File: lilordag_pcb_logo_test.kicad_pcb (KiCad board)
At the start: 2 copper layers, 98.1 x 100 mm, 178 parts, among them J1 USB4105-GF-A, J2 826629-7, J3 826629-7, Q1 BC846, Q2 BC846, Q3 MMBT3906, Q4 MMBT3906, Q5 BC846, Q6 BC846, Q7 SSM3J56MFV, Q8 SSM3J56MFV, SW1 PCM12SMTR, SW2 PCM12SMTR, SW3 SW_MEC_5G, SW4 PCM12SMTR, SW5 SW_MEC_5G, SW6 SW_MEC_5G, SW7 SW_MEC_5G, U1 ESP32-C3-MINI-1-N4, U2 WS2812B-B, U3 WS2812B-B, U4 WS2812B-B, U5 WS2812B-B

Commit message: Logos locked
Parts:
- moved Ref** 23.2 mm to (76.9, 123.0)
- moved Ref** 16.1 mm to (77.0, 103.2)
- moved Ref** 5.02 mm to (89.4, 91.5)
- moved Ref** 4.76 mm to (111.7, 91.5)
- moved Ref** 4.67 mm to (66.3, 91.5)
- moved Ref** 4.47 mm to (95.2, 77.2)
- moved Ref** 4.47 mm to (117.6, 77.2)
- moved Ref** 4.16 mm to (43.5, 91.5)
- moved Ref** 4.13 mm to (72.1, 77.2)
- moved Ref** 4.08 mm to (49.5, 77.2)
- moved Ref** 1.27 mm to (77.0, 112.5)
- moved Ref** 0.12 mm to (55.2, 114.0)
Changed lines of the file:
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@@
     )
   )
-  (footprint "pcb_logos:candy-simple-light-green" (layer "F.Cu")
-    (at 71.628 73.152)
+  (footprint "pcb_logos:candy-simple-light-green" locked (layer "F.Cu")
+    (at 72.1 77.25)
     (attr through_hole)
     (fp_text reference "Ref**" (at 0 0) (layer "F.SilkS") hide
@@
       ) (layer "F.Cu") (width 0.01) (fill solid))
   )
-  (footprint "pcb_logos:candy-simple-white" (layer "F.Cu")
-    (at 49.45 73.168839)
+  (footprint "pcb_logos:candy-simple-white" locked (layer "F.Cu")
+    (at 49.45 77.25)
     (attr through_hole)
     (fp_text reference "Ref**" (at 0 0) (layer "F.SilkS") hide
@@
     )
   )
-  (footprint "pcb_logos:drawing" (layer "F.Cu")
-    (at 76.962 99.822)
+  (footprint "pcb_logos:drawing" locked (layer "F.Cu")
+    (at 76.9 123)
     (attr through_hole)
     (fp_text reference "Ref**" (at 0 0) (layer "F.SilkS") hide
@@
     )
   )
-  (footprint "pcb_logos:candy-simple-clear" (layer "F.Cu")
-    (at 116.586 72.898)
+  (footprint "pcb_logos:candy-simple-clear" locked (layer "F.Cu")
+    (at 117.6 77.25)
     (attr through_hole)
     (fp_text reference "Ref**" (at 0 0) (layer "F.SilkS") hide
@@
     )
   )
-  (footprint "pcb_logos:simple_tower_7x7" (layer "F.Cu")
-    (at 77.216 111.252)
+  (footprint "pcb_logos:simple_tower_7x7" locked (layer "F.Cu")
+    (at 77 112.5)
     (attr through_hole)
     (fp_text reference "Ref**" (at 0 0) (layer "F.SilkS") hide
@@
     )
   )
-  (footprint "pcb_logos:tower-complex-gold" (layer "F.Cu")
-    (at 90.654962 86.684281)
+  (footprint "pcb_logos:tower-complex-gold" locked (layer "F.Cu")
+    (at 89.4 91.54)
     (attr through_hole)
     (fp_text reference "Ref**" (at 0 0) (layer "F.SilkS") hide
@@
       (net 79 "Net-(TP15-Pad1)") (pinfunction "DIN") (pintype "input"))
   )
-  (footprint "pcb_logos:candy-simple-gold" (layer "F.Cu")
-    (at 96.254379 72.894768)
+  (footprint "pcb_logos:candy-simple-gold" locked (layer "F.Cu")
+    (at 95.25 77.25)
     (attr through_hole)
     (fp_text reference "Ref**" (at 0 0) (layer "F.SilkS") hide
@@
     (pad "" np_thru_hole circle locked (at 0 0) (size 6 6) (drill 6) (layers *.Cu *.Mask))
   )
-  (footprint "pcb_logos:tower-complex-clear" (layer "F.Cu")
-    (at 110.722834 86.879447)
+  (footprint "pcb_logos:tower-complex-clear" locked (layer "F.Cu")
+    (at 111.7 91.54)
     (attr through_hole)
     (fp_text reference "Ref**" (at 0 0) (layer "F.SilkS") hide
@@
     )
   )
-  (footprint "pcb_logos:tower-complex-white" (layer "F.Cu")
-    (at 43.45 87.376)
+  (footprint "pcb_logos:tower-complex-white" locked (layer "F.Cu")
+    (at 43.45 91.54)
     (attr through_hole)
     (fp_text reference "Ref**" (at 0 0) (layer "F.SilkS") hide
@@
   )
   (footprint "pcb_logos:tower-complex-light-green-stars" locked (layer "F.Cu")
-    (at 55.1 114)
+    (at 55.225 114)
     (attr through_hole)
     (fp_text reference "Ref**" (at 0 0) (layer "F.SilkS") hide
@@
     )
   )
-  (footprint "pcb_logos:tower-complex-light-green" (layer "F.Cu")
-    (at 66.294 86.868)
+  (footprint "pcb_logos:tower-complex-light-green" locked (layer "F.Cu")
+    (at 66.3 91.54)
     (attr through_hole)
     (fp_text reference "Ref**" (at 0 0) (layer "F.SilkS") hide
@@
       ) (layer "F.Cu") (width 0.01) (fill solid))
   )
-  (footprint "pcb_logos:simple_tower_5x5" (layer "F.Cu")
-    (at 76.962 119.38)
+  (footprint "pcb_logos:simple_tower_5x5" locked (layer "F.Cu")
+    (at 77 103.25)
     (attr through_hole)
     (fp_text reference "Ref**" (at 0 0) (layer "F.SilkS") hide

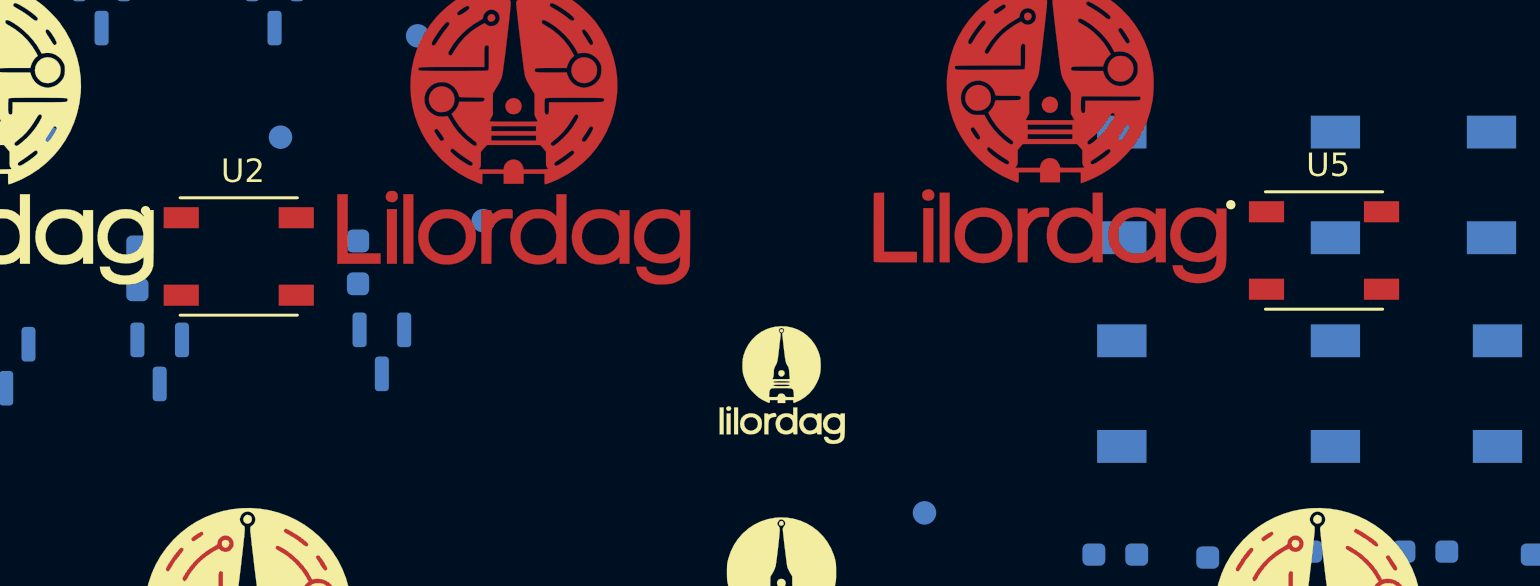
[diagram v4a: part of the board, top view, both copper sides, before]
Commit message: Added 3d model for RGBs
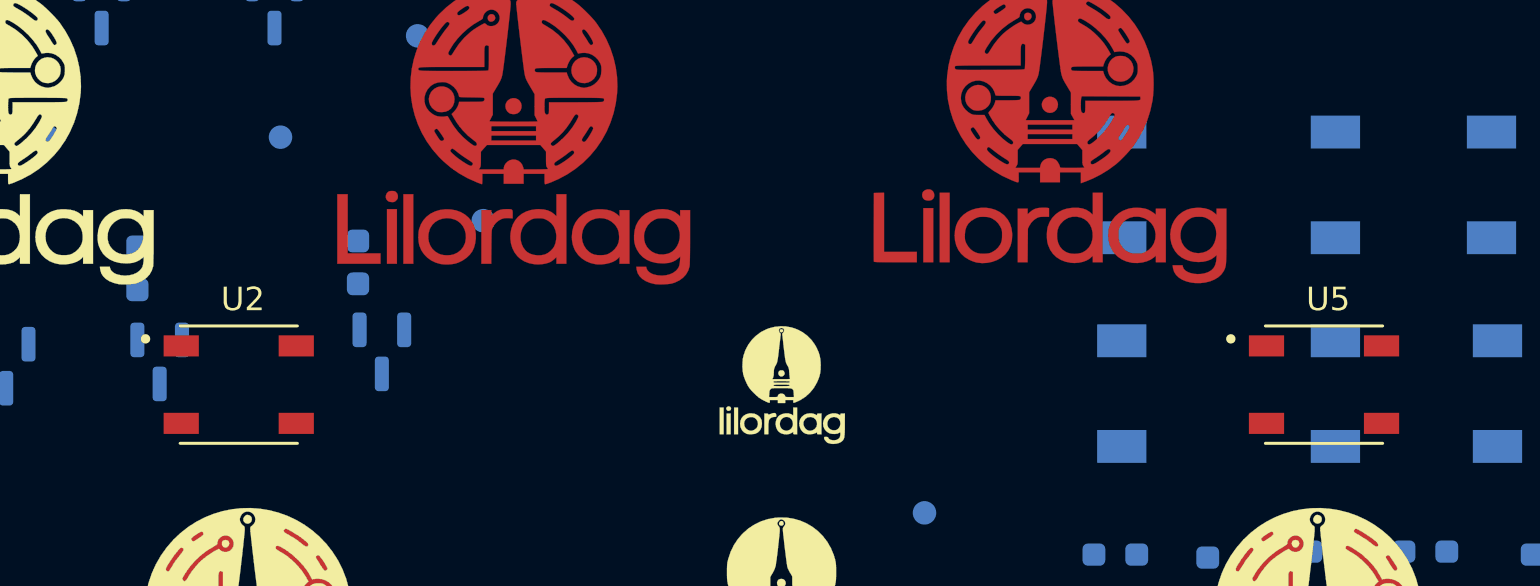
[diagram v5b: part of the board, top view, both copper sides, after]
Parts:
- moved U5 5.71 mm to (100.1, 103.2)
- moved U2 5.46 mm to (53.8, 103.2)
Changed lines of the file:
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@@
     (pad "4" smd rect locked (at 2.45 -1.65 180) (size 1.5 0.9) (layers "F.Cu" "F.Paste" "F.Mask")
       (net 83 "Net-(TP16-Pad1)") (pinfunction "DIN") (pintype "input"))
+    (model "${KIPRJMOD}/parts/WS2812B/WS2812B-B.step"
+      (offset (xyz 0 0 0))
+      (scale (xyz 1 1 1))
+      (rotate (xyz -90 0 0))
+    )
   )
   (footprint "pcb_logos:tower-complex-golden-stars" locked (layer "F.Cu")
@@
   )
   (footprint "WS2812B:LED_WS2812B-B" (layer "F.Cu")
-    (at 53.848 97.79)
+    (at 53.848 103.25)
     (property "MANUFACTURER" "Worldsemi")
     (property "MAXIMUM_PACKAGE_HIEGHT" "1.62 mm")
@@
     (pad "4" smd rect locked (at 2.45 -1.65 180) (size 1.5 0.9) (layers "F.Cu" "F.Paste" "F.Mask")
       (net 103 "RGB") (pinfunction "DIN") (pintype "input"))
+    (model "${KIPRJMOD}/parts/WS2812B/WS2812B-B.step"
+      (offset (xyz 0 0 0))
+      (scale (xyz 1 1 1))
+      (rotate (xyz -90 0 0))
+    )
   )
   (footprint "LED_SMD:LED_0603_1608Metric_Pad1.05x0.95mm_HandSolder" (layer "F.Cu")
@@
   )
   (footprint "WS2812B:LED_WS2812B-B" (layer "F.Cu")
-    (at 100.076 97.536)
+    (at 100.076 103.25)
     (property "MANUFACTURER" "Worldsemi")
     (property "MAXIMUM_PACKAGE_HIEGHT" "1.62 mm")
@@
     (pad "4" smd rect locked (at 2.45 -1.65 180) (size 1.5 0.9) (layers "F.Cu" "F.Paste" "F.Mask")
       (net 104 "Net-(TP17-Pad1)") (pinfunction "DIN") (pintype "input"))
+    (model "${KIPRJMOD}/parts/WS2812B/WS2812B-B.step"
+      (offset (xyz 0 0 0))
+      (scale (xyz 1 1 1))
+      (rotate (xyz -90 0 0))
+    )
   )
   (footprint "LED_SMD:LED_0603_1608Metric_Pad1.05x0.95mm_HandSolder" (layer "F.Cu")
@@
     (pad "4" smd rect locked (at 2.45 -1.65 180) (size 1.5 0.9) (layers "F.Cu" "F.Paste" "F.Mask")
       (net 79 "Net-(TP15-Pad1)") (pinfunction "DIN") (pintype "input"))
+    (model "${KIPRJMOD}/parts/WS2812B/WS2812B-B.step"
+      (offset (xyz 0 0 0))
+      (scale (xyz 1 1 1))
+      (rotate (xyz -90 0 0))
+    )
   )
   (footprint "pcb_logos:candy-simple-gold" locked (layer "F.Cu")

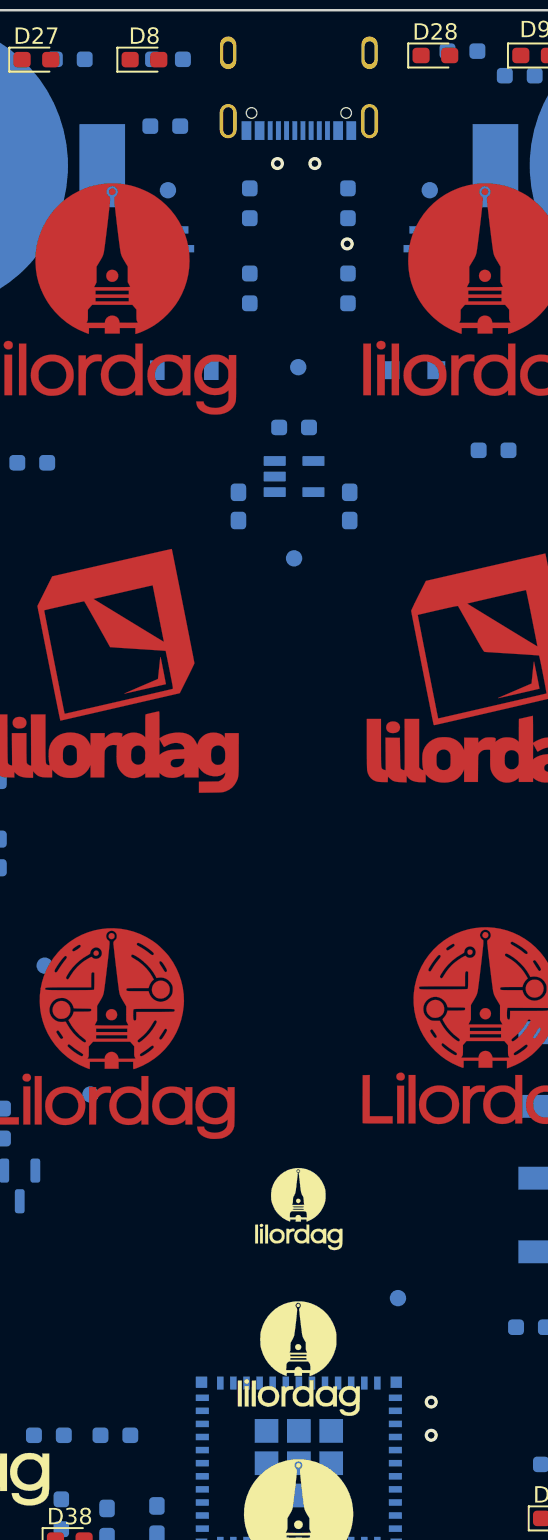
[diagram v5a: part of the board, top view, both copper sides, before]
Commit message: USB and battery power installed
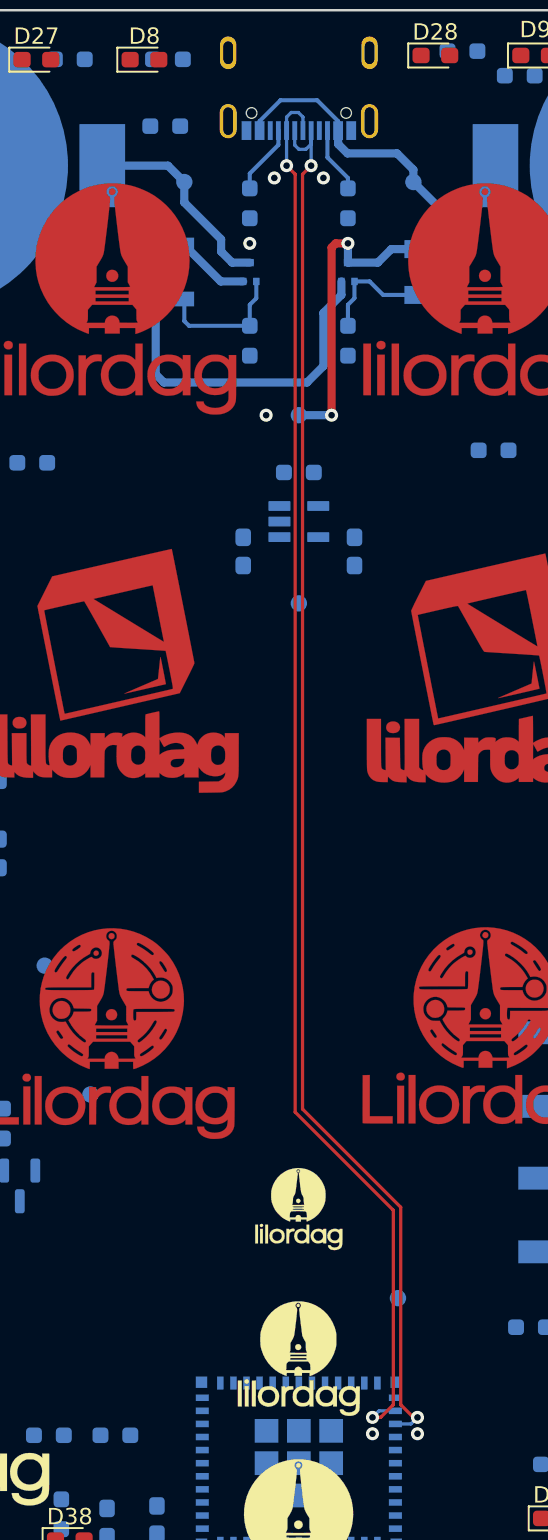
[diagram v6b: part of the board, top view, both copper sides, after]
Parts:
- moved D43 6.00 mm to (70.0, 46.0), turned to -90 degrees
- moved D44 6.00 mm to (84.0, 46.0), turned to -90 degrees
- moved Q7 4.47 mm to (74.0, 46.0)
- moved Q8 4.47 mm to (80.0, 46.0)
- moved R52 3.20 mm to (74.0, 50.2), turned to -90 degrees
- moved R53 3.20 mm to (80.0, 50.2), turned to -90 degrees
- moved TP12 2.93 mm to (77.0, 54.8)
- moved 3.3V 2.77 mm to (77.0, 66.2)
- moved C2 2.77 mm to (80.4, 63.1)
- moved R47 2.77 mm to (77.0, 58.2)
- moved VR1 2.77 mm to (77.0, 61.2)
- moved C1 2.77 mm to (73.6, 63.1)
- moved 5V 1.12 mm to (84.0, 40.5)
- moved BATT 1.12 mm to (70.0, 40.5)
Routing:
- net USB_D-: track 0.00 -> 86.6 mm
- net USB_D+: track 0.00 -> 86.4 mm
- net +BATT: track 0.00 -> 30.4 mm
- net +5V: track 0.00 -> 30.0 mm
- net VCC: track 0.00 -> 18.9 mm, vias 0 -> 2
- net Net-(BT1-Pad1): track 0.00 -> 12.6 mm
- net Net-(D43-Pad2): track 0.00 -> 8.35 mm
- net Net-(J1-PadA5): track 0.00 -> 4.26 mm
- net Net-(J1-PadB5): track 0.00 -> 4.05 mm
- net GND: vias 0 -> 6
- net (no net): vias 1 -> 0

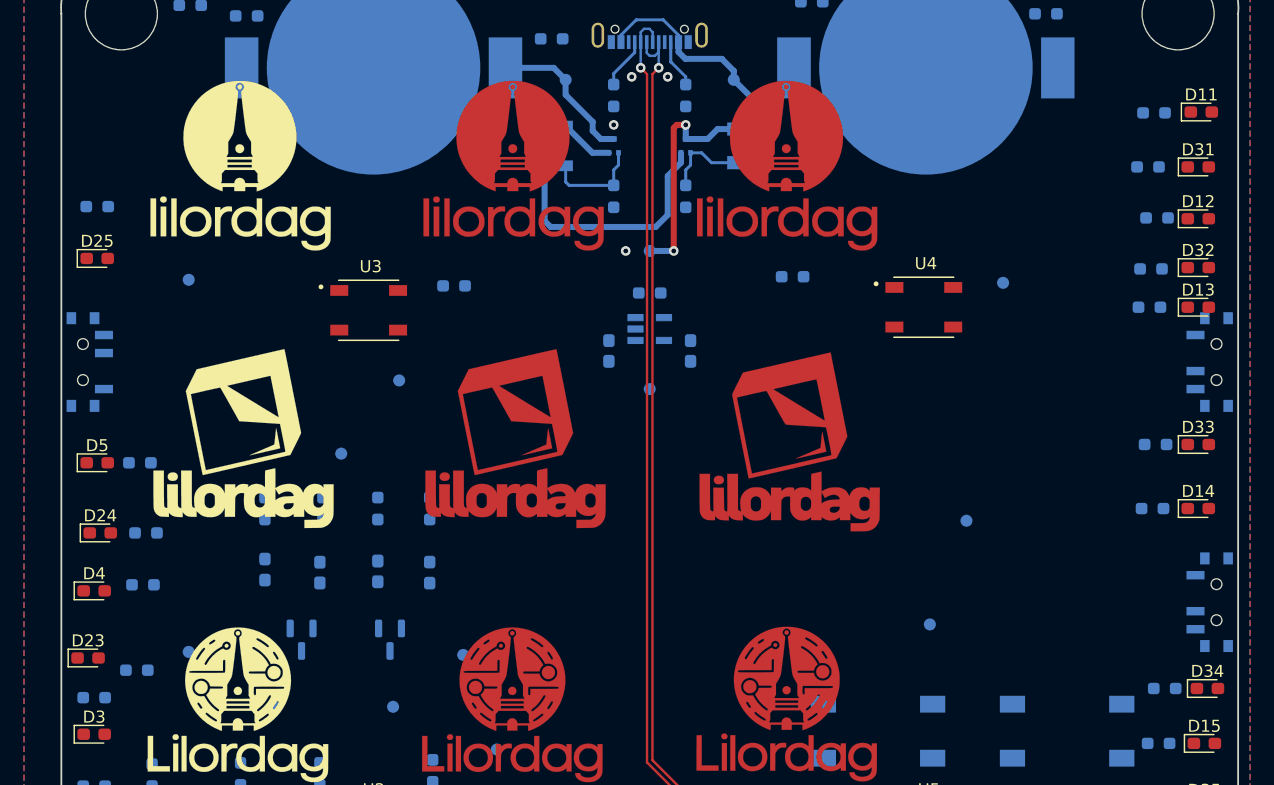
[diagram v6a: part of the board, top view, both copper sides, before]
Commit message: Vibrator wired in
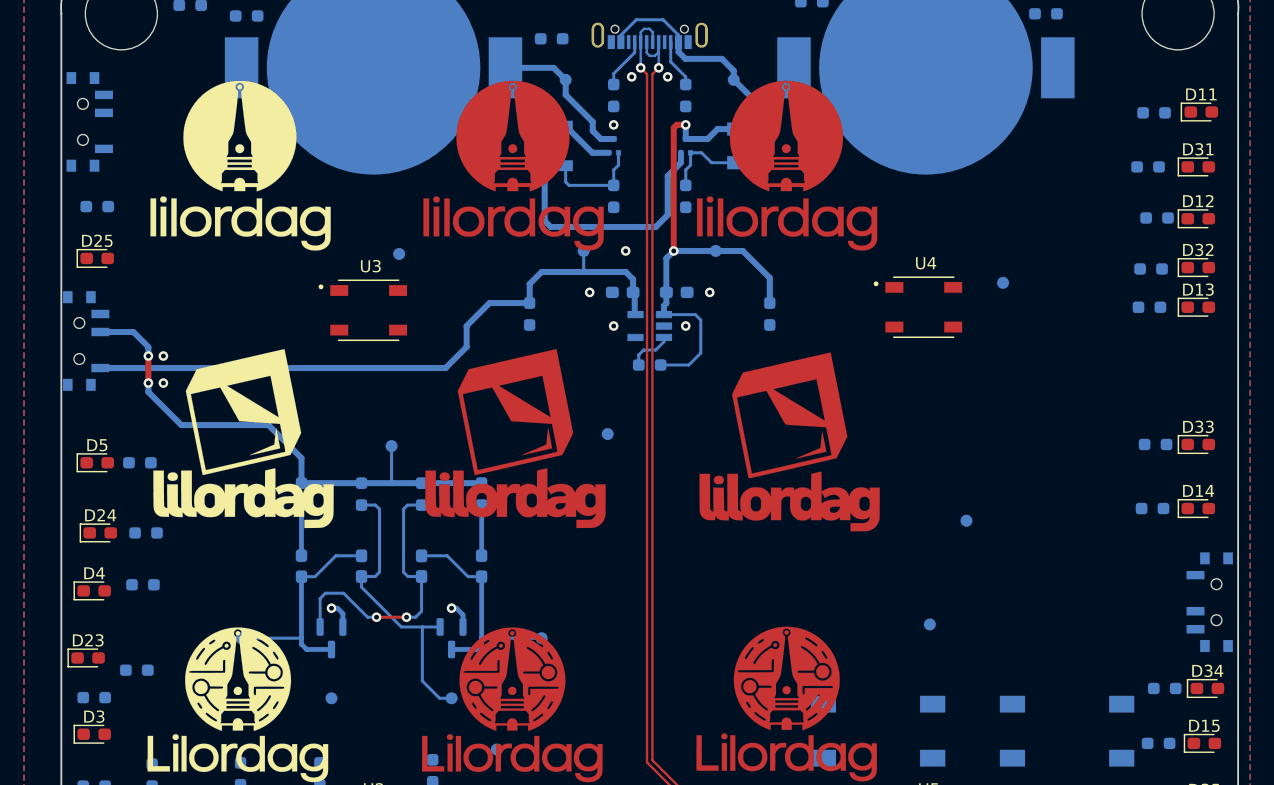
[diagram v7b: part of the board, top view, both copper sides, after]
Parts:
- moved SW2 94.7 mm to (29.5, 62.2), turned to 90 degrees
- moved TP3 37.2 mm to (73.5, 70.0)
- moved SW4 20.0 mm to (29.8, 44.0)
- moved 3.3V 12.7 mm to (71.5, 54.8)
- moved TP15 10.5 mm to (56.1, 55.0)
- moved C1 7.46 mm to (79.2, 58.2), turned to 0 degrees
- moved C2 7.46 mm to (74.8, 58.2), turned to 180 degrees
- moved R58 6.72 mm to (67.0, 60.0), turned to 90 degrees
- moved LEF_COL 6.68 mm to (68.0, 87.0)
- moved R47 6.00 mm to (77.0, 64.2), turned to 180 degrees
- moved VCC 5.50 mm to (82.5, 54.8)
- moved Q5 5.13 mm to (60.5, 87.0)
- moved LEFT_BASE 4.93 mm to (60.5, 92.0)
- moved RIGHT_BASE 4.83 mm to (50.5, 92.0)
- moved RIGHT_COL 4.54 mm to (43.0, 87.0)
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- renumbered TP12 to VCC
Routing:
- net +3.3V: track 0.00 -> 54.8 mm
- net V3.3-VIBRATOR: track 0.00 -> 43.5 mm, vias 0 -> 2
- net LEFT_BASE: track 0.00 -> 24.9 mm
- net VCC: track 18.9 -> 43.3 mm
- net RIGHT_BASE: track 0.00 -> 23.5 mm, vias 0 -> 2
- net RIGHT_LED_CONNECTION: track 0.00 -> 19.0 mm
- net LEFT_LED_CONNECTION: track 0.00 -> 19.0 mm
- net GND: track 0.00 -> 4.44 mm, vias 6 -> 14
- net Net-(D42-Pad2): track 0.00 -> 4.21 mm
- net Net-(D41-Pad2): track 0.00 -> 4.21 mm
- net Net-(R47-Pad2): track 0.00 -> 3.75 mm

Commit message: Breakout wired in
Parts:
- ESP 3.3: renamed from TP11
- moved SW1 95.1 mm to (29.5, 75.5), turned to 90 degrees
- moved ESP 58.0 mm to (29.5, 102.0)
- moved ESP 3.3 48.6 mm to (35.5, 98.8)
- moved R44 41.7 mm to (28.2, 135.2)
- moved R23 41.4 mm to (24.5, 135.2)
- moved R45 38.8 mm to (20.8, 135.2)
- moved R24 38.4 mm to (17.2, 135.5)
- moved D38 37.8 mm to (28.2, 138.5)
- moved Q1 36.9 mm to (55.5, 138.5)
- moved R10 36.9 mm to (54.4, 134.7)
- moved Q2 36.1 mm to (37.2, 138.2)
- moved Q3 36.0 mm to (49.5, 138.2)
- moved R31 36.0 mm to (48.5, 134.2)
- moved D19 35.9 mm to (24.6, 138.5)
- moved R33 35.8 mm to (41.7, 134.1)
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- renumbered SW4 to ESP
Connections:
- J2 pad 3: BOOT -> IO7
- J2 pad 4: ENABLE -> STRAP_IO8
- J2 pad 5: RX -> BOOT
- J2 pad 6: TX -> RX
- J2 pad 7: STRAP_IO8 -> TX
- J3 pad 1: IO0 -> IO6
- J3 pad 2: IO1 -> IO5
- J3 pad 3: LEFT_LED_CONNECTION -> RIGHT_LED_CONNECTION
- J3 pad 4: RIGHT_LED_CONNECTION -> IO1
- J3 pad 5: IO5 -> IO0
- J3 pad 6: IO6 -> ENABLE
- J3 pad 7: IO7 -> LEFT_LED_CONNECTION
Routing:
- net +3.3V: track 54.8 -> 145.7 mm, vias 0 -> 2
- net V3.3-ESP: track 0.00 -> 60.3 mm, vias 0 -> 2
- net IO6: track 0.00 -> 56.7 mm
- net IO5: track 0.00 -> 51.4 mm
- net RIGHT_LED_CONNECTION: track 19.0 -> 66.2 mm
- net LEFT_BASE: track 24.9 -> 67.5 mm
- net RIGHT_BASE: track 23.5 -> 65.9 mm
- net IO7: track 0.00 -> 40.8 mm
- net IO1: track 0.00 -> 39.5 mm
- net STRAP_IO8: track 0.00 -> 35.5 mm
- net IO0: track 0.00 -> 35.1 mm
- net BOOT: track 0.00 -> 29.8 mm
- net ENABLE: track 0.00 -> 28.1 mm, vias 0 -> 1
- net LEFT_LED_CONNECTION: track 19.0 -> 41.8 mm
- net RX: track 0.00 -> 20.5 mm
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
